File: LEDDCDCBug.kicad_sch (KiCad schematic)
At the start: 18 parts, among them J1 Conn_01x01, J2 Conn_01x01, J3 Conn_01x01, J4 Conn_01x01, J5 Conn_01x01, J6 Conn_01x01, J7 Conn_01x01, J8 Conn_01x01

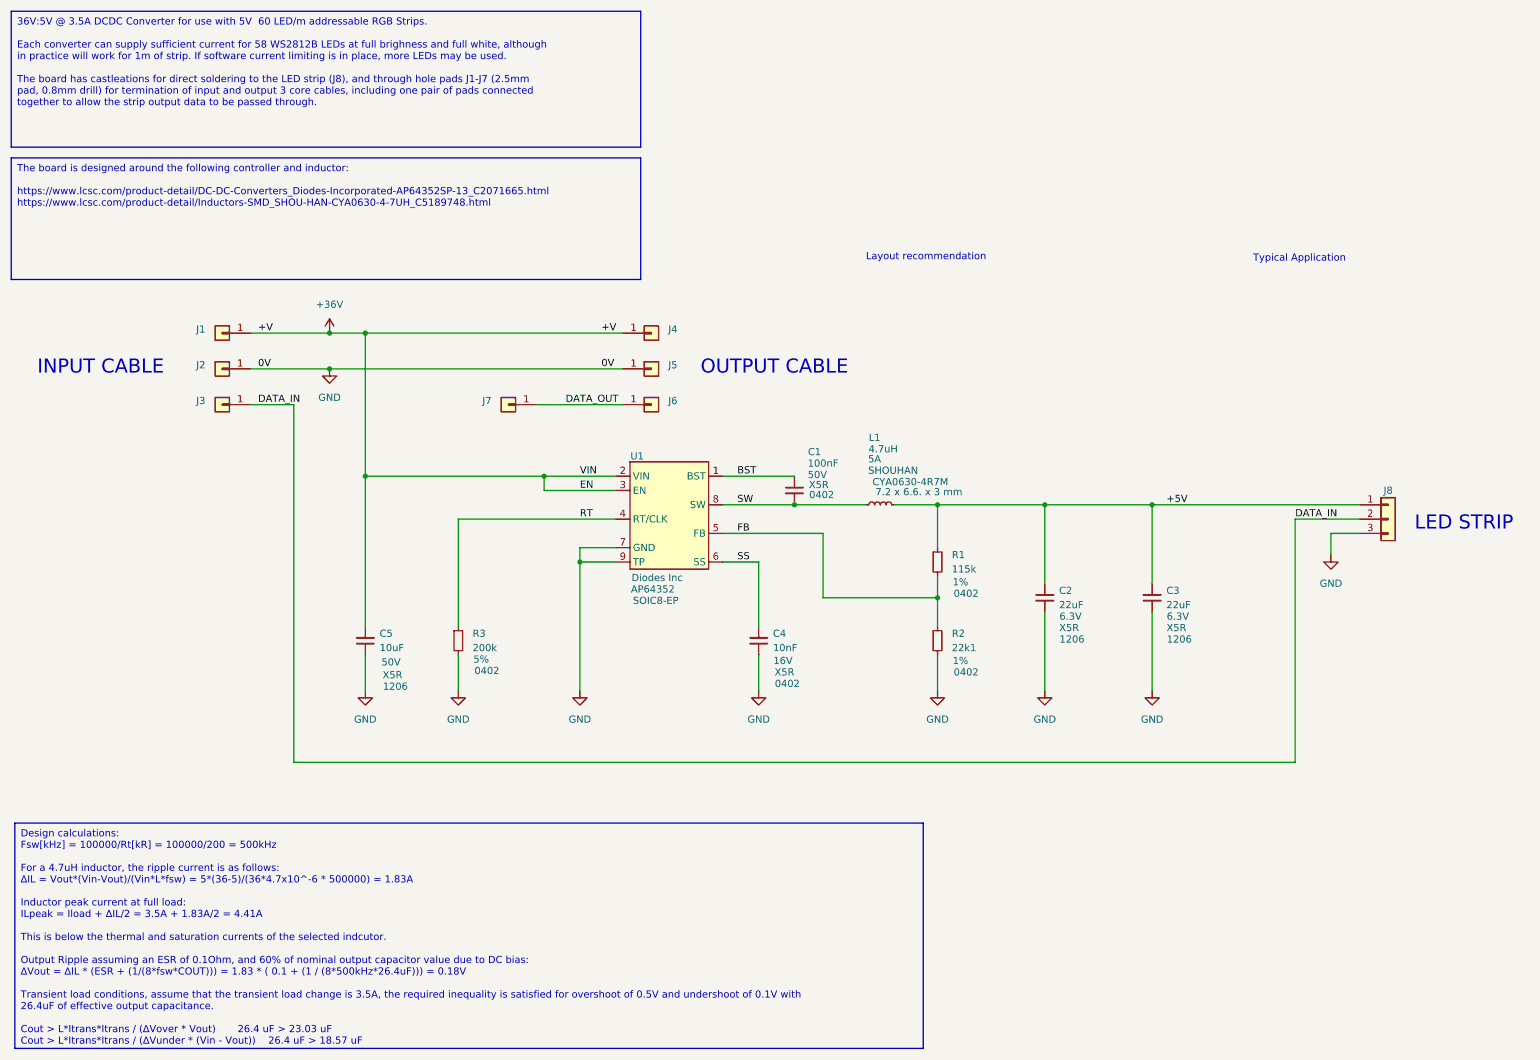
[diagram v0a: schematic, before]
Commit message: update design calcs based on real component data
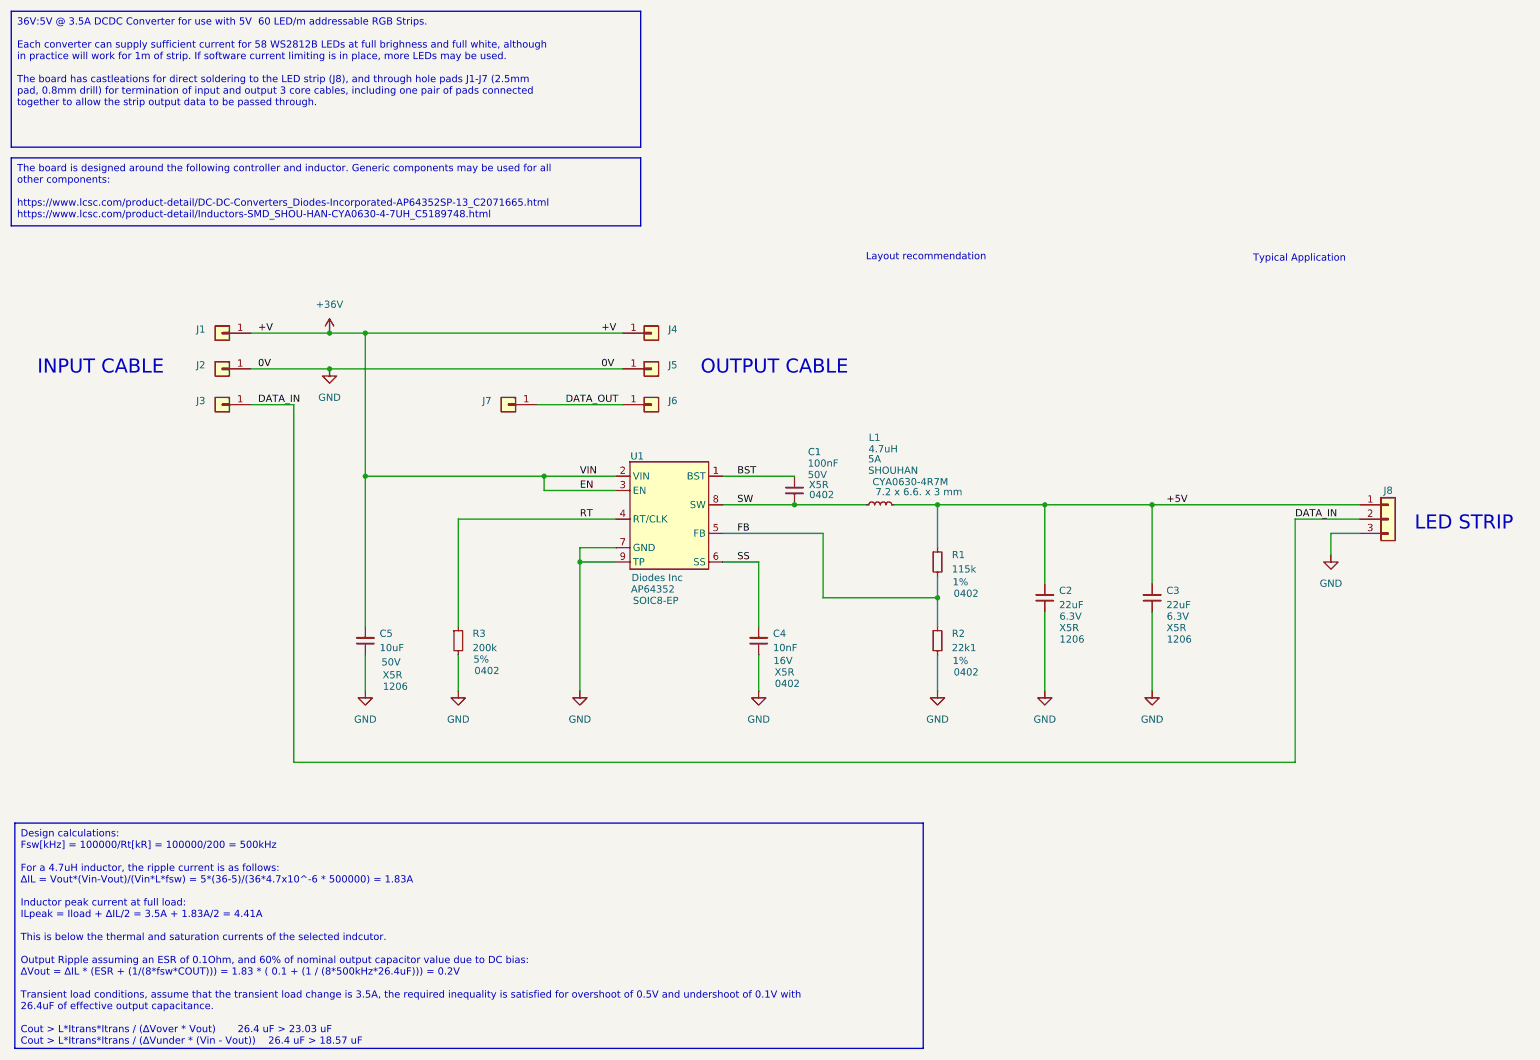
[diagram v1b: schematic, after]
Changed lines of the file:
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@@
 		)
 	)
-	(text_box "Design calculations:\nFsw[kHz] = 100000/Rt[kR] = 100000/200 = 500kHz\n\nFor a 4.7uH inductor, the ripple current is as follows:\n∆IL = Vout*(Vin-Vout)/(Vin*L*fsw) = 5*(36-5)/(36*4.7x10^-6 * 500000) = 1.83A\n\nInductor peak current at full load:\nILpeak = Iload + ∆IL/2 = 3.5A + 1.83A/2 = 4.41A\n\nThis is below the thermal and saturation currents of the selected indcutor.\n\nOutput Ripple assuming an ESR of 0.1Ohm, and 60% of nominal output capacitor value due to DC bias:\n∆Vout = ∆IL * (ESR + (1/(8*fsw*COUT))) = 1.83 * ( 0.1 + (1 / (8*500kHz*26.4uF))) = 0.18V\n\nTransient load conditions, assume that the transient load change is 3.5A, the required inequality is satisfied for overshoot of 0.5V and undershoot of 0.1V with 26.4uF of effective output capacitance.\n\nCout > L*Itrans*Itrans / (∆Vover * Vout)       26.4 uF > 23.03 uF\nCout > L*Itrans*Itrans / (∆Vunder * (Vin - Vout))    26.4 uF > 18.57 uF"
+	(text_box "Design calculations:\nFsw[kHz] = 100000/Rt[kR] = 100000/200 = 500kHz\n\nFor a 4.7uH inductor, the ripple current is as follows:\n∆IL = Vout*(Vin-Vout)/(Vin*L*fsw) = 5*(36-5)/(36*4.7x10^-6 * 500000) = 1.83A\n\nInductor peak current at full load:\nILpeak = Iload + ∆IL/2 = 3.5A + 1.83A/2 = 4.41A\n\nThis is below the thermal and saturation currents of the selected indcutor.\n\nOutput Ripple assuming an ESR of 0.1Ohm, and 60% of nominal output capacitor value due to DC bias:\n∆Vout = ∆IL * (ESR + (1/(8*fsw*COUT))) = 1.83 * ( 0.1 + (1 / (8*500kHz*26.4uF))) = 0.2V\n\nTransient load conditions, assume that the transient load change is 3.5A, the required inequality is satisfied for overshoot of 0.5V and undershoot of 0.1V with 26.4uF of effective output capacitance.\n\nCout > L*Itrans*Itrans / (∆Vover * Vout)       26.4 uF > 23.03 uF\nCout > L*Itrans*Itrans / (∆Vunder * (Vin - Vout))    26.4 uF > 18.57 uF"
 		(exclude_from_sim no)
 		(at 13.97 156.845 0)
@@
 		)
 	)
-	(text_box "The board is designed around the following controller and inductor:\n\nhttps://www.lcsc.com/product-detail/DC-DC-Converters_Diodes-Incorporated-AP64352SP-13_C2071665.html\nhttps://www.lcsc.com/product-detail/Inductors-SMD_SHOU-HAN-CYA0630-4-7UH_C5189748.html"
+	(text_box "The board is designed around the following controller and inductor. Generic components may be used for all other components:\n\nhttps://www.lcsc.com/product-detail/DC-DC-Converters_Diodes-Incorporated-AP64352SP-13_C2071665.html\nhttps://www.lcsc.com/product-detail/Inductors-SMD_SHOU-HAN-CYA0630-4-7UH_C5189748.html"
 		(exclude_from_sim no)
 		(at 13.335 38.735 0)
-		(size 111.76 21.59)
+		(size 111.76 12.065)
 		(stroke
 			(width 0)

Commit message: add title block
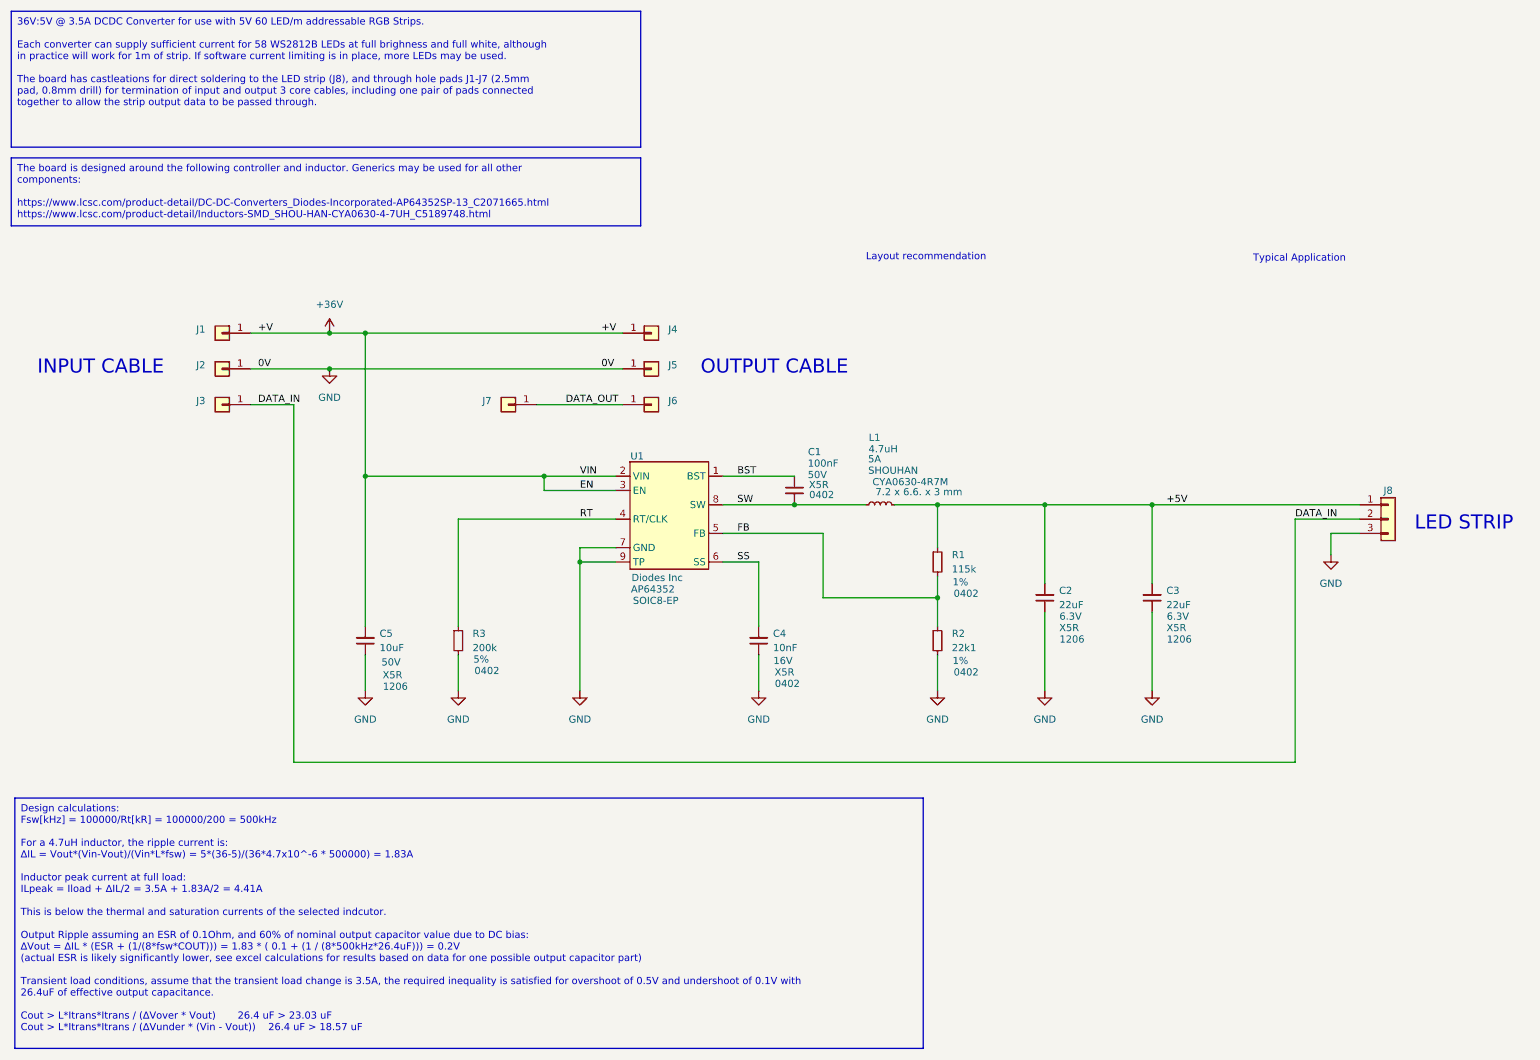
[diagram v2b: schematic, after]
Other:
- company: (none) -> Sturdy Pete Electronics
- title: (none) -> DCD Bug
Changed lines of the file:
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@@
 	(generator_version "8.0")
 	(paper "A4")
+	(title_block
+		(title "DCD Bug")
+		(date "2025-05-16")
+		(rev "V1")
+		(company "Sturdy Pete Electronics")
+		(comment 1 "Engineering by Chris Boyce")
+		(comment 2 "36V:5V @ 3.5A DCDC Converter for use with 5V  60 LED/m addressable RGB Strips.")
+	)
 	(junction
 		(at 152.4 100.33)
@@
 		)
 	)
-	(text_box "Design calculations:\nFsw[kHz] = 100000/Rt[kR] = 100000/200 = 500kHz\n\nFor a 4.7uH inductor, the ripple current is as follows:\n∆IL = Vout*(Vin-Vout)/(Vin*L*fsw) = 5*(36-5)/(36*4.7x10^-6 * 500000) = 1.83A\n\nInductor peak current at full load:\nILpeak = Iload + ∆IL/2 = 3.5A + 1.83A/2 = 4.41A\n\nThis is below the thermal and saturation currents of the selected indcutor.\n\nOutput Ripple assuming an ESR of 0.1Ohm, and 60% of nominal output capacitor value due to DC bias:\n∆Vout = ∆IL * (ESR + (1/(8*fsw*COUT))) = 1.83 * ( 0.1 + (1 / (8*500kHz*26.4uF))) = 0.2V\n\nTransient load conditions, assume that the transient load change is 3.5A, the required inequality is satisfied for overshoot of 0.5V and undershoot of 0.1V with 26.4uF of effective output capacitance.\n\nCout > L*Itrans*Itrans / (∆Vover * Vout)       26.4 uF > 23.03 uF\nCout > L*Itrans*Itrans / (∆Vunder * (Vin - Vout))    26.4 uF > 18.57 uF"
+	(text_box "Design calculations:\nFsw[kHz] = 100000/Rt[kR] = 100000/200 = 500kHz\n\nFor a 4.7uH inductor, the ripple current is:\n∆IL = Vout*(Vin-Vout)/(Vin*L*fsw) = 5*(36-5)/(36*4.7x10^-6 * 500000) = 1.83A\n\nInductor peak current at full load:\nILpeak = Iload + ∆IL/2 = 3.5A + 1.83A/2 = 4.41A\n\nThis is below the thermal and saturation currents of the selected indcutor.\n\nOutput Ripple assuming an ESR of 0.1Ohm, and 60% of nominal output capacitor value due to DC bias:\n∆Vout = ∆IL * (ESR + (1/(8*fsw*COUT))) = 1.83 * ( 0.1 + (1 / (8*500kHz*26.4uF))) = 0.2V\n(actual ESR is likely significantly lower, see excel calculations for results based on data for one possible output capacitor part)\n\nTransient load conditions, assume that the transient load change is 3.5A, the required inequality is satisfied for overshoot of 0.5V and undershoot of 0.1V with 26.4uF of effective output capacitance.\n\nCout > L*Itrans*Itrans / (∆Vover * Vout)       26.4 uF > 23.03 uF\nCout > L*Itrans*Itrans / (∆Vunder * (Vin - Vout))    26.4 uF > 18.57 uF"
 		(exclude_from_sim no)
-		(at 13.97 156.845 0)
-		(size 161.29 40.005)
+		(at 13.97 152.4 0)
+		(size 161.29 44.45)
 		(stroke
 			(width 0)
@@
 		)
 		(fill
-			(type none)
+			(type color)
+			(color 213 237 255 1)
 		)
 		(effects
@@
 		)
 	)
-	(text_box "The board is designed around the following controller and inductor. Generic components may be used for all other components:\n\nhttps://www.lcsc.com/product-detail/DC-DC-Converters_Diodes-Incorporated-AP64352SP-13_C2071665.html\nhttps://www.lcsc.com/product-detail/Inductors-SMD_SHOU-HAN-CYA0630-4-7UH_C5189748.html"
+	(text_box "The board is designed around the following controller and inductor. Generics may be used for all other components:\n\nhttps://www.lcsc.com/product-detail/DC-DC-Converters_Diodes-Incorporated-AP64352SP-13_C2071665.html\nhttps://www.lcsc.com/product-detail/Inductors-SMD_SHOU-HAN-CYA0630-4-7UH_C5189748.html"
 		(exclude_from_sim no)
 		(at 13.335 38.735 0)
@@
 		)
 		(fill
-			(type none)
+			(type color)
+			(color 214 238 255 1)
 		)
 		(effects
@@
 		)
 	)
-	(text_box "36V:5V @ 3.5A DCDC Converter for use with 5V  60 LED/m addressable RGB Strips.\n\nEach converter can supply sufficient current for 58 WS2812B LEDs at full brighness and full white, although in practice will work for 1m of strip. If software current limiting is in place, more LEDs may be used.\n\nThe board has castleations for direct soldering to the LED strip (J8), and through hole pads J1-J7 (2.5mm pad, 0.8mm drill) for termination of input and output 3 core cables, including one pair of pads connected together to allow the strip output data to be passed through."
+	(text_box "36V:5V @ 3.5A DCDC Converter for use with 5V 60 LED/m addressable RGB Strips.\n\nEach converter can supply sufficient current for 58 WS2812B LEDs at full brighness and full white, although in practice will work for 1m of strip. If software current limiting is in place, more LEDs may be used.\n\nThe board has castleations for direct soldering to the LED strip (J8), and through hole pads J1-J7 (2.5mm pad, 0.8mm drill) for termination of input and output 3 core cables, including one pair of pads connected together to allow the strip output data to be passed through."
 		(exclude_from_sim no)
 		(at 13.335 12.7 0)
@@
 		)
 		(fill
-			(type none)
+			(type color)
+			(color 214 238 255 1)
 		)
 		(effects
